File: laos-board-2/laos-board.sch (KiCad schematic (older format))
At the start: 89 parts, among them IC1 KB847, IC2 KB847, J1 USB-A, J10 CONN_4, J11 MBED NXP, J12 JP, J13 JP_3, J14 CONN_4, J15 JP, J16 JP_3, J17 POLOLU1201, J18 CONN_5, J19 JP, J2 CONN_4, J20 JP_3, J21 JP, J22 JP_3, J23 POLOLU1201, J24 CONN_5, J25 JP, J26 JP_3, J27 CONN_4, J28 JP3, J29 CONN_4, J3 JP, J30 JP, J31 JP_3, J32 POLOLU1201, J33 CONN_5, J34 CONN_4, J35 JP, J36 JP_3, J37 CONN_4, J38 CONN_2, J39 CONN_4, J4 MAGJACK, J5 CONN_2, J6 JP, J7 JP_3, J8 POLOLU1201, J9 CONN_5, Q1 TIP115, Q2 TIP115, U1 65HVD251, U2 SDCARD, U3 7805

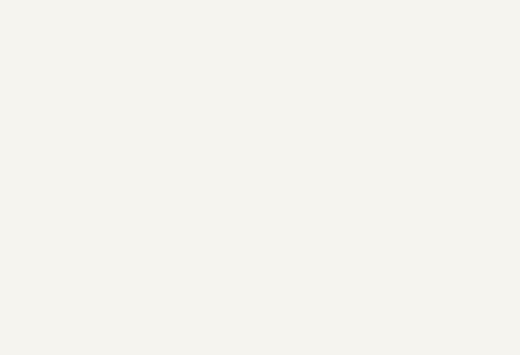
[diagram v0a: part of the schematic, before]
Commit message: Initial work on module placement
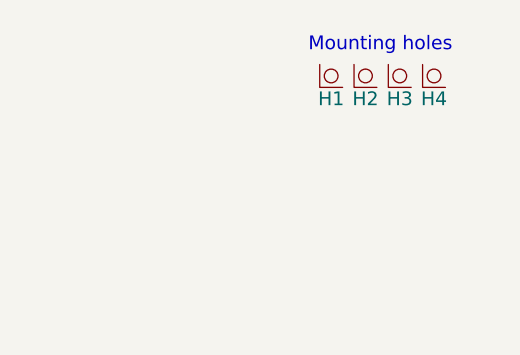
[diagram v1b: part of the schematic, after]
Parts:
- added H1, H2, H3, H4: MOUNT_HOLE, symbol MOUNT_HOLE
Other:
- note added: "Mounting holes"
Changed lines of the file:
@@
-EESchema Schematic File Version 2  date Sat 02 Jul 2011 03:50:09 PM CEST
+EESchema Schematic File Version 2  date Wed 06 Jul 2011 12:54:18 PM CEST
 LIBS:laos_kicad_lib
+LIBS:conn
+LIBS:74xx
+LIBS:adc-dac
+LIBS:analog_switches
+LIBS:atmel
+LIBS:bjt
+LIBS:can
+LIBS:capacitive
+LIBS:cmos4000
+LIBS:device
+LIBS:digital-audio
+LIBS:digpot
+LIBS:diode
+LIBS:display
+LIBS:fet
+LIBS:figaro
+LIBS:graphic
+LIBS:hc11
+LIBS:i2c
+LIBS:inductive
+LIBS:intel
+LIBS:interface
+LIBS:linear
+LIBS:mech_switch
+LIBS:memory
+LIBS:microchip
+LIBS:opto
+LIBS:periph
+LIBS:power
+LIBS:power_switches
+LIBS:protection
+LIBS:pspice
+LIBS:radio
+LIBS:regul
+LIBS:renesas
+LIBS:resist
+LIBS:supervisor
+LIBS:switcher
+LIBS:video
 LIBS:laos-board-cache
 EELAYER 25  0
@@
 Sheet 1 1
 Title "LAOS"
-Date "1 jul 2011"
+Date "6 jul 2011"
 Rev "1"
 Comp "http://www.laoslaser.org"
@@
 Comment4 ""
 $EndDescr
+Text Notes 15300 700  0    60   ~ 0
+Mounting holes
+$Comp
+L MOUNT_HOLE H4
+U 1 1 4E1435F8
+P 15900 850
+F 0 "H4" H 15850 800 60  0000 C CNN
+F 1 "MOUNT_HOLE" H 15900 1100 60  0001 C CNN
+	1    15900 850
+	1    0    0    -1
+$EndComp
+$Comp
+L MOUNT_HOLE H3
+U 1 1 4E1435F7
+P 15750 850
+F 0 "H3" H 15700 800 60  0000 C CNN
+F 1 "MOUNT_HOLE" H 15750 1100 60  0001 C CNN
+	1    15750 850
+	1    0    0    -1
+$EndComp
+$Comp
+L MOUNT_HOLE H2
+U 1 1 4E1435F4
+P 15600 850
+F 0 "H2" H 15550 800 60  0000 C CNN
+F 1 "MOUNT_HOLE" H 15600 1100 60  0001 C CNN
+	1    15600 850
+	1    0    0    -1
+$EndComp
+$Comp
+L MOUNT_HOLE H1
+U 1 1 4E1435EA
+P 15450 850
+F 0 "H1" H 15400 800 60  0000 C CNN
+F 1 "MOUNT_HOLE" H 15450 1100 60  0001 C CNN
+	1    15450 850
+	1    0    0    -1
+$EndComp
 Wire Wire Line
 	2550 7200 2550 7160
@@
 $EndComp
 $Comp
-L GND #PWR49
+L GND #PWR51
 U 1 1 4E0DFD98
 P 2200 7250
-F 0 "#PWR49" H 2200 7250 30  0001 C CNN
+F 0 "#PWR51" H 2200 7250 30  0001 C CNN
 F 1 "GND" H 2200 7180 30  0001 C CNN
 	1    2200 7250
@@
 $EndComp
 $Comp
-L +5V #PWR50
+L +5V #PWR49
 U 1 1 4E0DF8E3
 P 2550 7160
-F 0 "#PWR50" H 2550 7250 20  0001 C CNN
+F 0 "#PWR49" H 2550 7250 20  0001 C CNN
 F 1 "+5V" H 2550 7250 30  0000 C CNN
 	1    2550 7160
@@
 $EndComp
 $Comp
-L VAA #PWR51
+L VAA #PWR50
 U 1 1 4E0B3045
 P 2680 7170
-F 0 "#PWR51" H 2680 7230 30  0001 C CNN
+F 0 "#PWR50" H 2680 7230 30  0001 C CNN
 F 1 "VAA" H 2680 7280 30  0000 C CNN
 	1    2680 7170

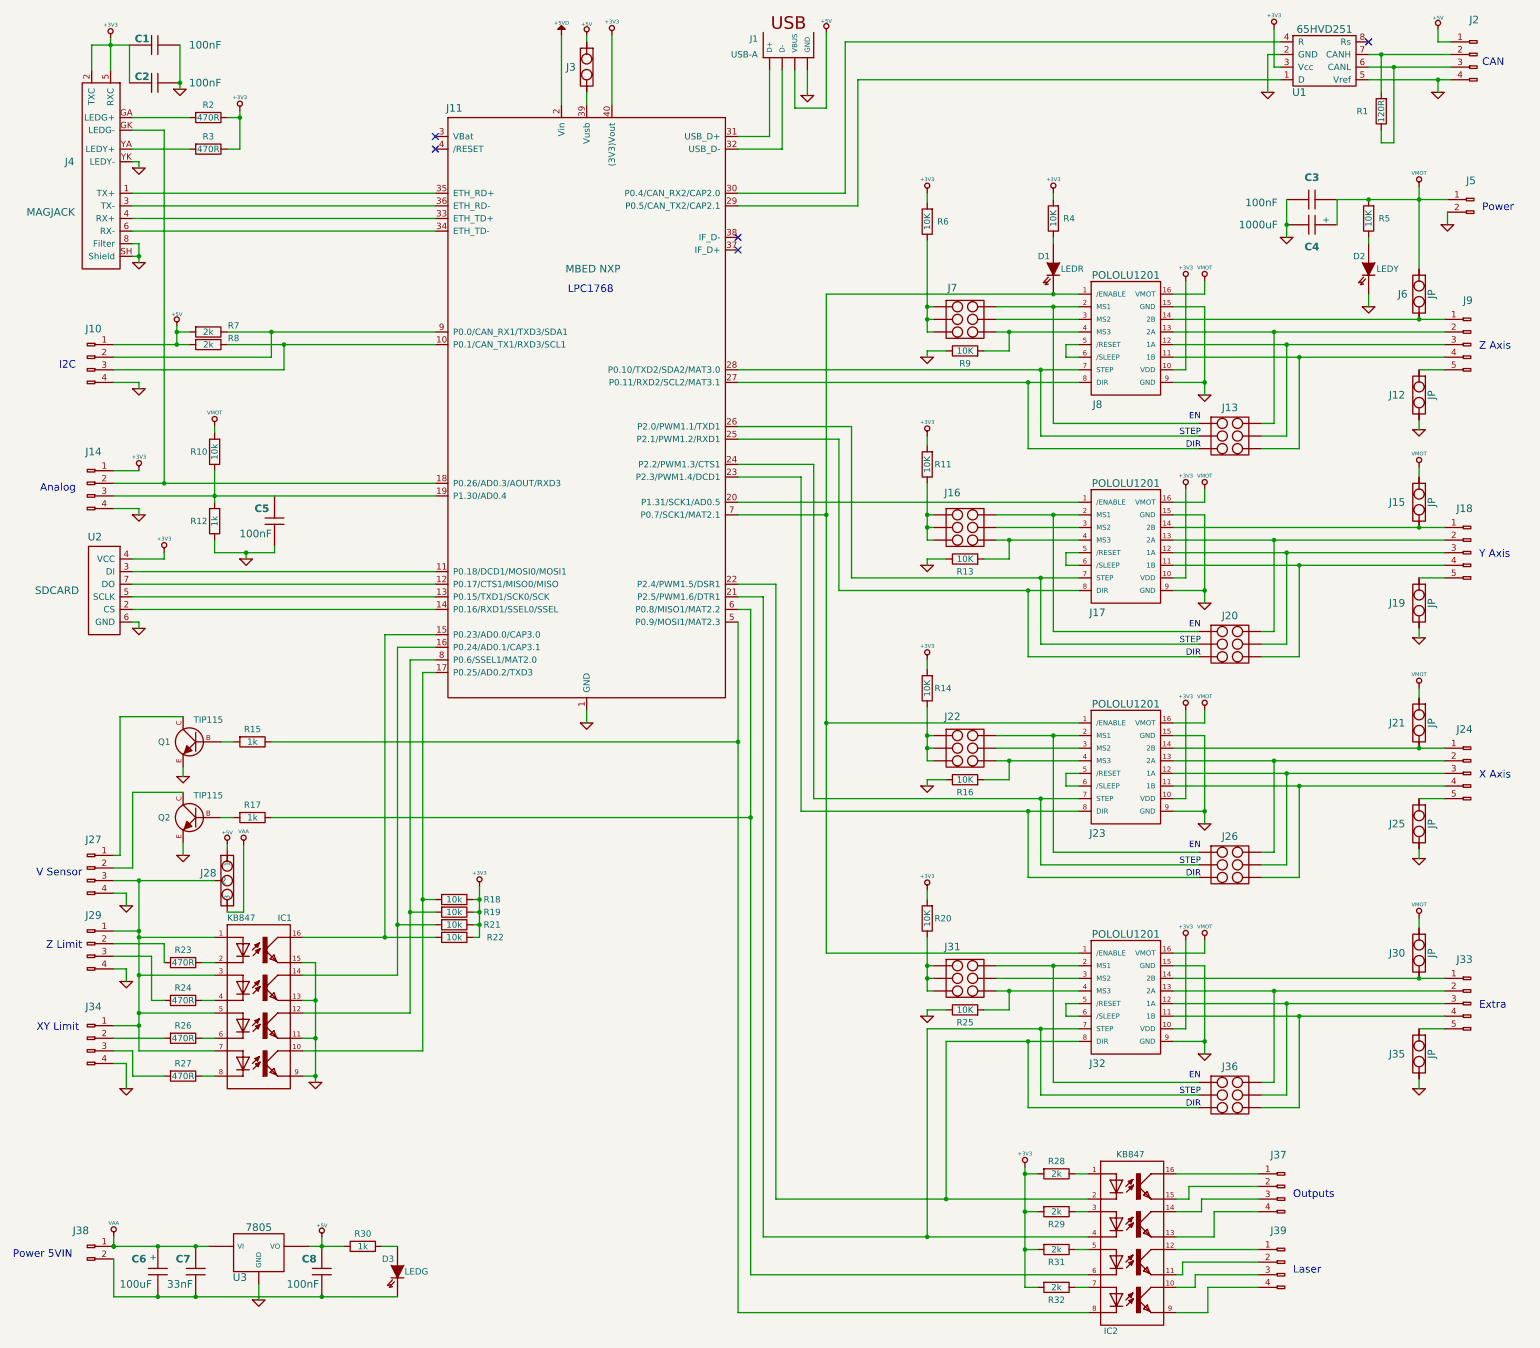
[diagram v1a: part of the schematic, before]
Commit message: More component placement
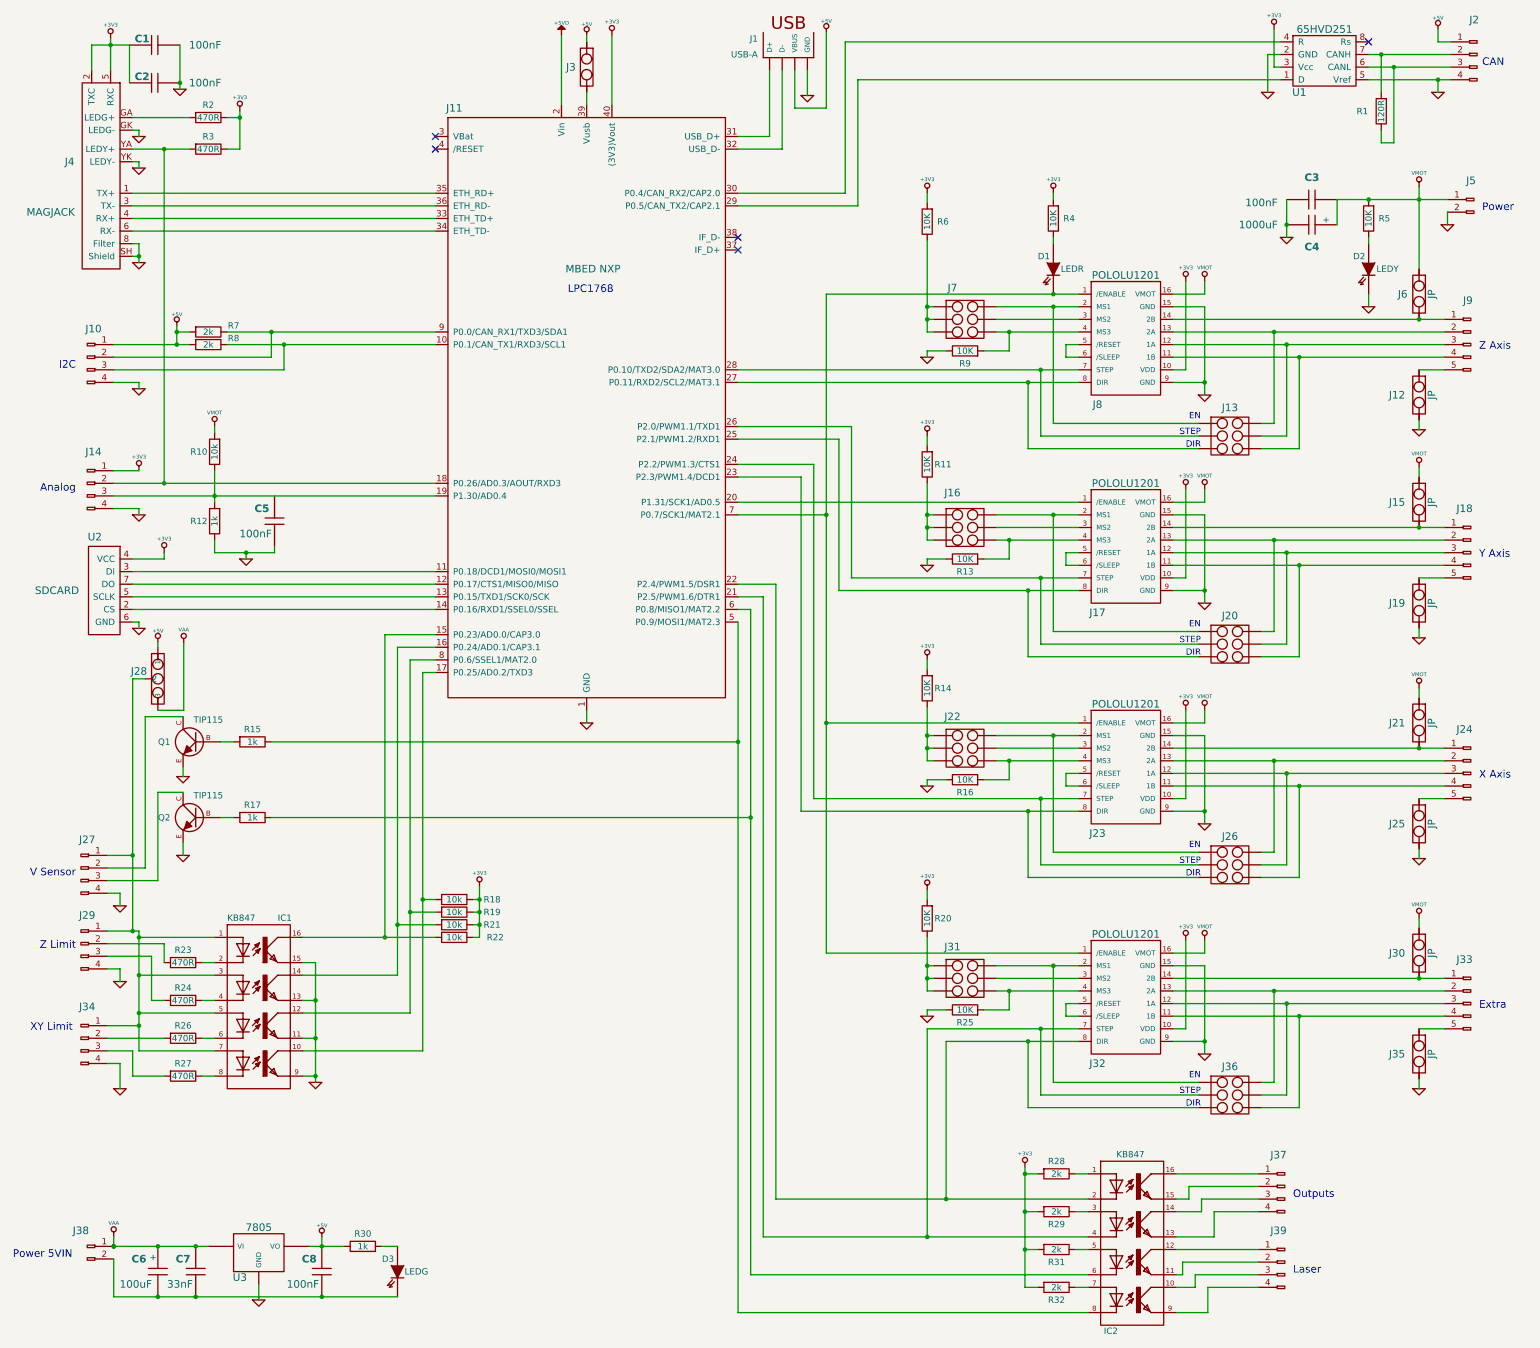
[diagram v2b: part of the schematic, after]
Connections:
- net GND: now also J4.GK (LEDG-)
- net at J11.18 (P0.26/AD0.3/AOUT/RXD3), J14.2 (P2): now also J4.YA (LEDY+), R3.2; no longer J4.GK (LEDG-)
- net at IC1.1, IC1.3 (A), IC1.5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: now also J27.1 (P1); no longer J27.3 (P3)
- net at Q2.C: now also J27.3 (P3); no longer J27.2 (P2)
- net at Q1.C: now also J27.2 (P2); no longer J27.1 (P1)
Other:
- moved on the sheet: J27, J28, J29, J34
